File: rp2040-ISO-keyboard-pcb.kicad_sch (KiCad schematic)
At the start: 82 parts, among them J1 USB_C_Receptacle_USB2.0, J2 Conn_01x04, U1 SRV05-4, U2 RP2040, U3 IS313741A, U4 XC6206, U5 W25Q128JVS, Y1 12MHz

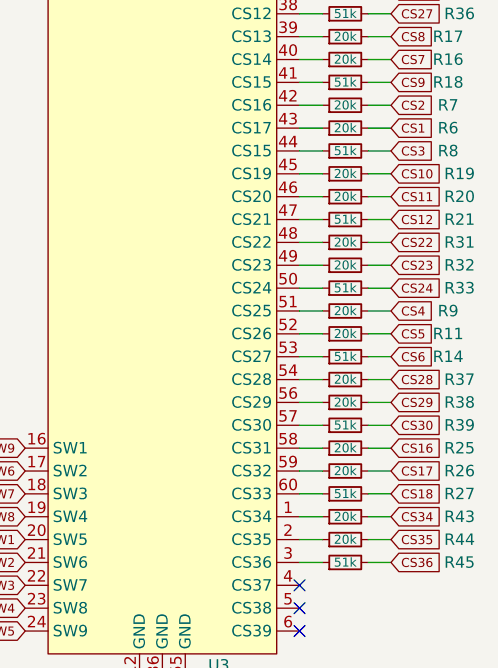
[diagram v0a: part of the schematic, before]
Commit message: added more routing
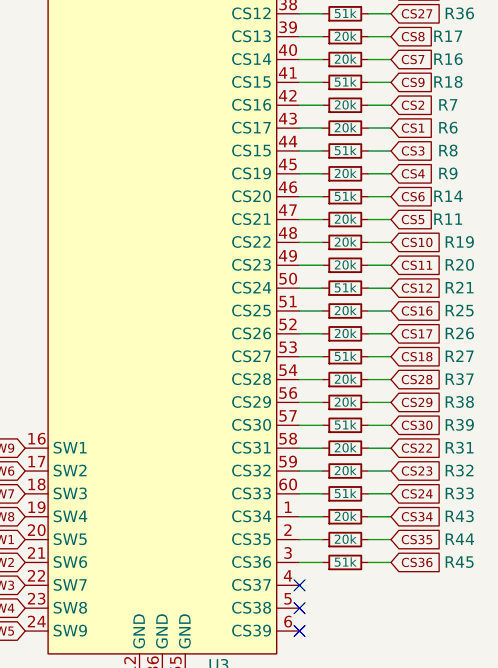
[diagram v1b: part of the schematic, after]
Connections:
- net at R26.1: now also U3.52 (CS26); no longer U3.59 (CS32)
- net at R32.1: now also U3.59 (CS32); no longer U3.49 (CS23)
- net at R20.1: now also U3.49 (CS23); no longer U3.46 (CS20)
- net at R14.1: now also U3.46 (CS20); no longer U3.53 (CS27)
- net at R31.1: now also U3.58 (CS31); no longer U3.48 (CS22)
- net at R21.1: now also U3.50 (CS24); no longer U3.47 (CS21)
- net at R9.1: now also U3.45 (CS19); no longer U3.51 (CS25)
- net at R25.1: now also U3.51 (CS25); no longer U3.58 (CS31)
- net at R33.1: now also U3.60 (CS33); no longer U3.50 (CS24)
- net at R27.1: now also U3.53 (CS27); no longer U3.60 (CS33)
- net at R19.1: now also U3.48 (CS22); no longer U3.45 (CS19)
- net at R11.1: now also U3.47 (CS21); no longer U3.52 (CS26)
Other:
- moved on the sheet: R11, R14, R19, R20, R21, R25, R26, R27, R31, R32, R33, R9

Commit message: routing finished
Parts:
- added C0: 22uf/10v, Capacitor_Tantalum_SMD:CP_EIA-3216-18_Kemet-A, symbol PCB-rescue:CP1-Device
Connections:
- net +5V: now also C0.1
- net GND: now also C0.2
- net at R43.1: now also U3.4 (CS37); no longer U3.1 (CS34)
- net at R39.1: now also U3.3 (CS36); no longer U3.57 (CS30)
- net at R37.1: now also U3.1 (CS34); no longer U3.54 (CS28)
- net at R44.1: now also U3.5 (CS38); no longer U3.2 (CS35)
- net at R38.1: now also U3.2 (CS35); no longer U3.56 (CS29)
- net at R45.1: now also U3.6 (CS39); no longer U3.3 (CS36)
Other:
- moved on the sheet: R37, R38, R39, R43, R44, R45

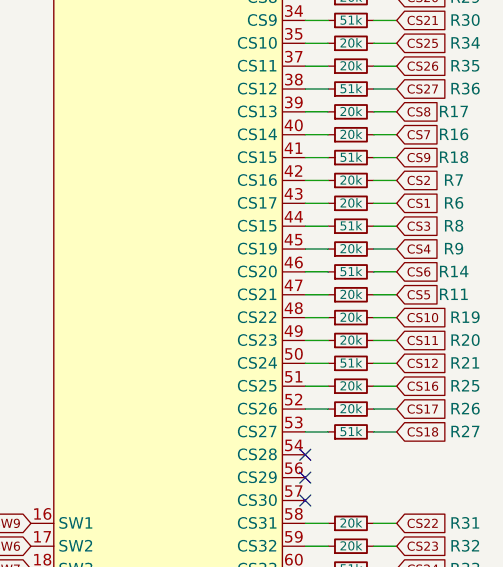
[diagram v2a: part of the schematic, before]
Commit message: cleaned up some routing and used smaller resistors (0402 instead of 0603)
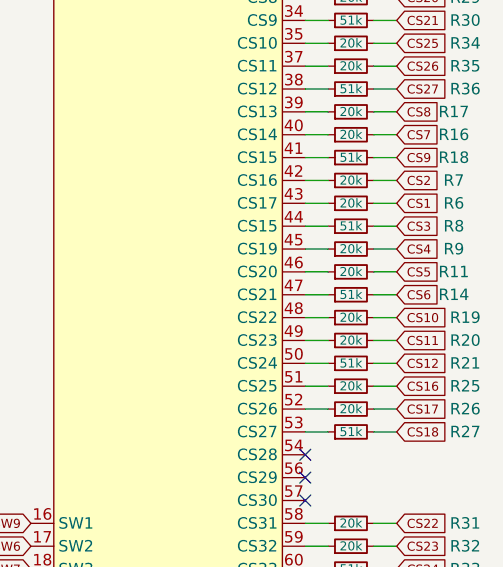
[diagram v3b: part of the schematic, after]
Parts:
- R10, R11, R13, R14, R16, R17, R18, R19, R2, R20, R21, R22, R23, R24, R25, R26, R27, R28, R29, R3, R30, R31, R32, R33, R34, R35, R36, R37, R38, R39, R40, R41, R42, R43, R44, R45, R6, R7, R8, R9: footprint Resistor_SMD:R_0603_1608Metric -> Resistor_SMD:R_0402_1005Metric
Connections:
- net at R14.1: now also U3.47 (CS21); no longer U3.46 (CS20)
- net at R11.1: now also U3.46 (CS20); no longer U3.47 (CS21)
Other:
- moved on the sheet: R11, R14

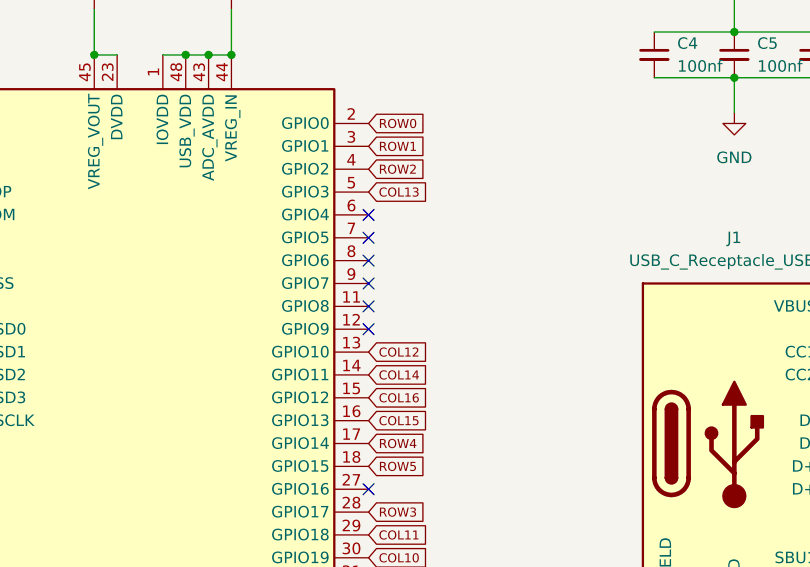
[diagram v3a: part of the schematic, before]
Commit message: added ground layers
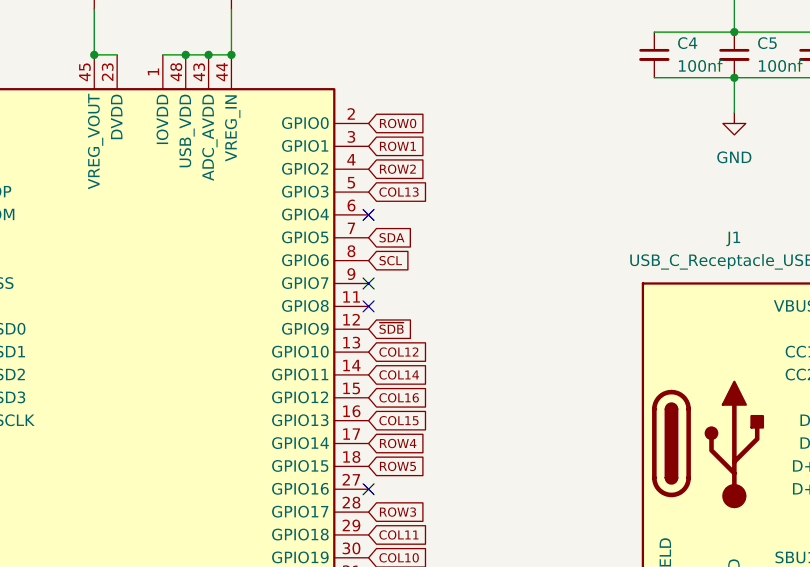
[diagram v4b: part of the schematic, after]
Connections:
- net SCL: now also U2.8 (GPIO6)
- net SDA: now also U2.7 (GPIO5)
- net ~{SDB}: now also U2.12 (GPIO9)
- no-connect marks 15 -> 12
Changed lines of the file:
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@@
   (no_connect (at 107.95 62.23))
   (no_connect (at 107.95 54.61))
-  (no_connect (at 107.95 67.31))
   (no_connect (at 163.83 92.71))
   (no_connect (at 163.83 95.25))
   (no_connect (at 330.2 131.445))
   (no_connect (at 107.95 85.09))
-  (no_connect (at 107.95 57.15))
   (no_connect (at 204.47 76.2))
   (no_connect (at 330.2 126.365))
-  (no_connect (at 107.95 59.69))
   (no_connect (at 299.72 62.865))
   (no_connect (at 330.2 128.905))
@@
     )
   )
+  (global_label "SCL" (shape input) (at 107.95 59.69 0) (fields_autoplaced)
+    (effects (font (size 1 1)) (justify left))
+    (property "Intersheet References" "${INTERSHEET_REFS}" (id 0) (at 112.6119 59.7525 0)
+      (effects (font (size 1 1)) (justify left) hide)
+    )
+  )
   (global_label "COL14" (shape input) (at 107.95 72.39 0) (fields_autoplaced)
     (effects (font (size 1 1)) (justify left))
@@
     )
   )
+  (global_label "SDA" (shape input) (at 107.95 57.15 0) (fields_autoplaced)
+    (effects (font (size 1 1)) (justify left))
+    (property "Intersheet References" "${INTERSHEET_REFS}" (id 0) (at 112.6595 57.2125 0)
+      (effects (font (size 1 1)) (justify left) hide)
+    )
+  )
   (global_label "CS23" (shape input) (at 340.36 136.525 0) (fields_autoplaced)
     (effects (font (size 1 1)) (justify left))
@@
       (effects (font (size 1 1)) (justify left) hide)
     )
+  )
+  (global_label "~{SDB}" (shape input) (at 107.95 67.31 0) (fields_autoplaced)
+    (effects (font (size 1 1)) (justify left))
+    (property "Intersheet References" "${INTERSHEET_REFS}" (id 0) (at 112.8024 67.2475 0)
+      (effects (font (size 1 1)) (justify left) hide)
+    )
